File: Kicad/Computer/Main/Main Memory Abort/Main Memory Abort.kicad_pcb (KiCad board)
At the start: 2 copper layers, 18.8 x 43.3 mm, 14 parts, among them IC1 AP7365-33WG-7, IC2 74LVC32APW,118, IC4 74LVC74APW,118, IC5 SN74CBT3257CPWR, IC7 74LVC11PW,112, J2 Conn_02x16_Counter_Clockwise

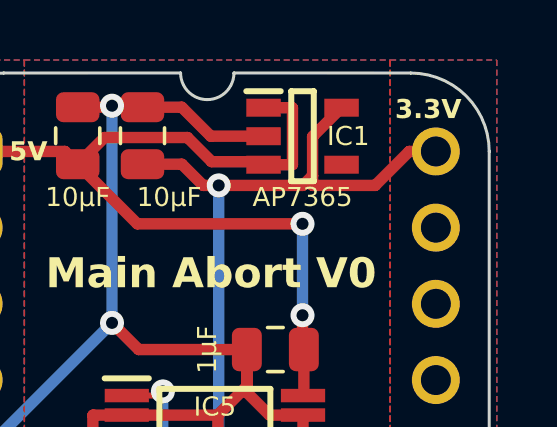
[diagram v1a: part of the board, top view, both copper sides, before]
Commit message: Added a (potentially) 50MHz board.
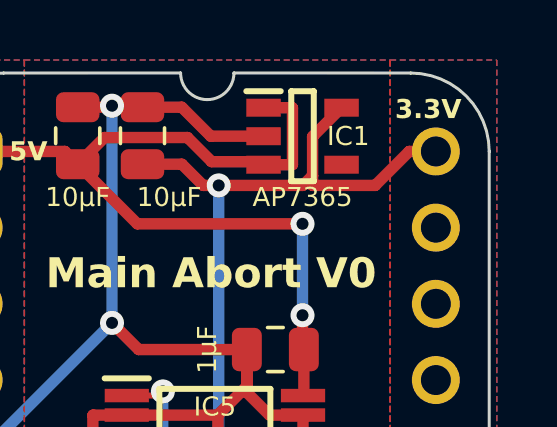
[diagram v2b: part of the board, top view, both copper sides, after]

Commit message: Started adding SD Card writing.
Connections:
- net ~{ABORT} renamed ~{Contention}
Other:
- board text added: "~{FAIL}"
- board text removed: "~{ABORT}"
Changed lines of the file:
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@@
 	(net 39 "~{Main}_{2}")
 	(net 40 "~{Reset}")
-	(net 41 "~{ABORT}")
+	(net 41 "~{Contention}")
 	(net 42 "~{Main}_{M}")
 	(footprint "SamacSys_Parts:C_0805"
@@
 		(fp_arc
 			(start 14.404267 -2.613733)
-			(mid 16.252453 -1.848189)
+			(mid 16.25245 -1.848186)
 			(end 17.017999 -0.000001)
 			(stroke
@@
 			(layers "*.Cu" "*.Mask")
 			(remove_unused_layers no)
-			(net 41 "~{ABORT}")
+			(net 41 "~{Contention}")
 			(pinfunction "Pin_19")
 			(pintype "passive")
@@
 			(size 0.45 1.475)
 			(layers "F.Cu" "F.Paste" "F.Mask")
-			(net 41 "~{ABORT}")
+			(net 41 "~{Contention}")
 			(pinfunction "~{1Q}")
 			(pintype "output")
@@
 		)
 	)
-	(gr_text "~{ABORT}"
+	(gr_text "~{FAIL}"
 		(at 103.124 91.44 0)
 		(layer "F.SilkS")

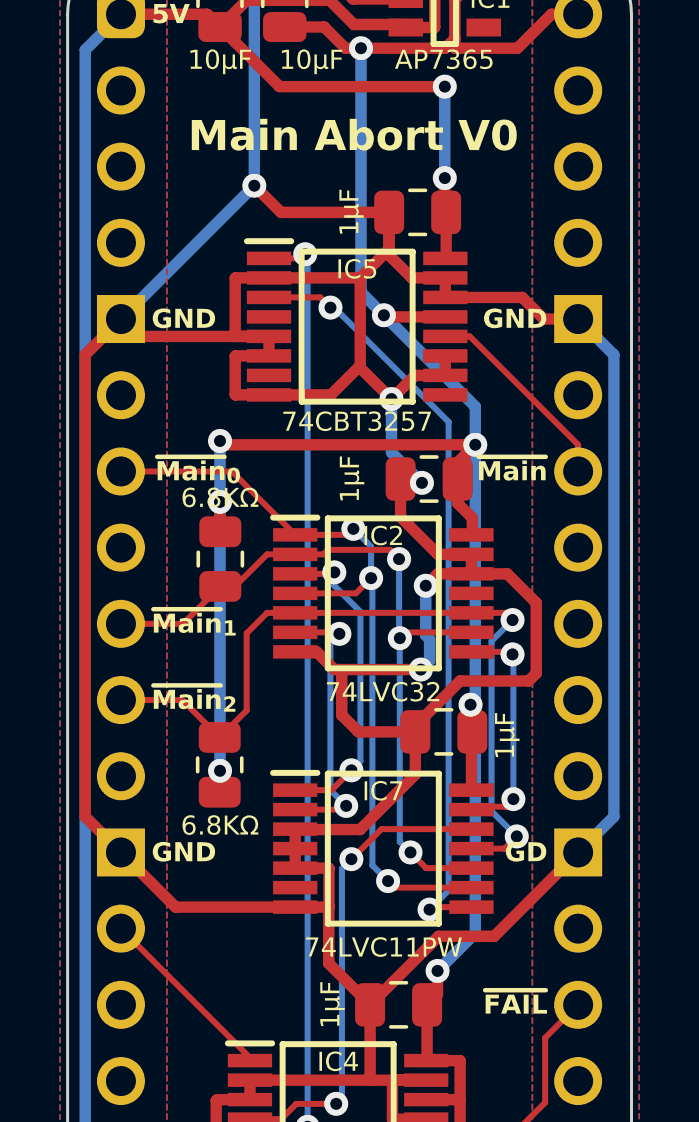
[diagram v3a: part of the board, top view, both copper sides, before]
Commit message: Added a TTL5V UART.
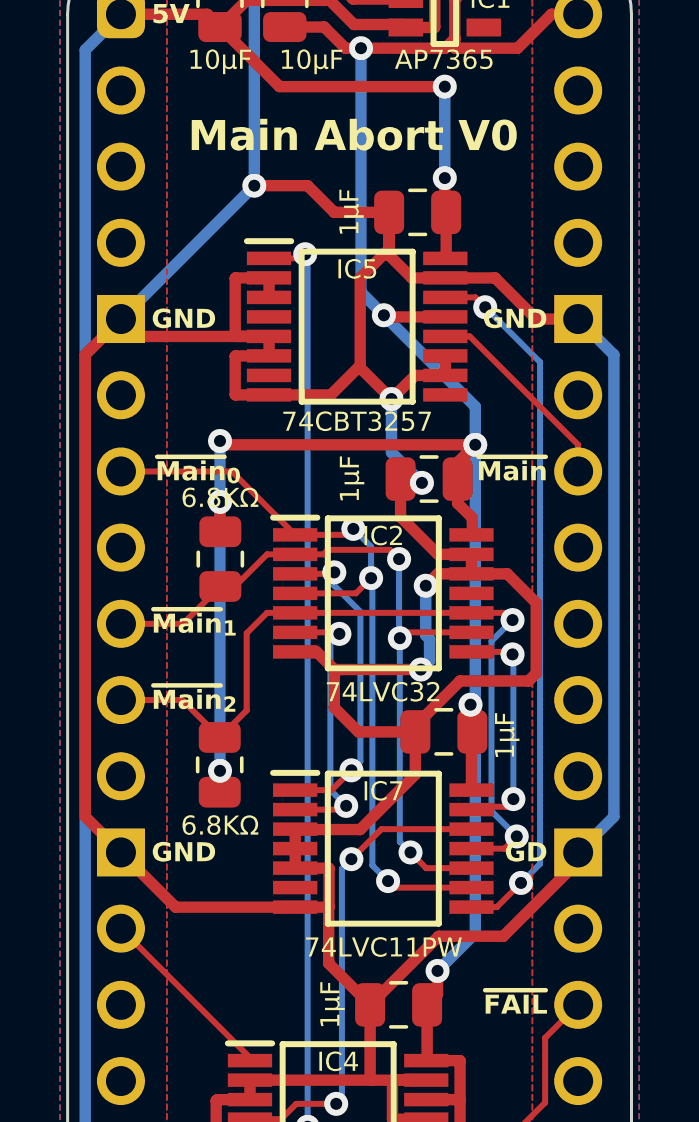
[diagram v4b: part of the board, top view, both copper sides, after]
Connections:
- net Net-(IC2-1Y) renamed /~{Main}+~{Main}_{1}
- net Net-(IC2-2Y) renamed /~{Main}+~{Main}_{2}
- net Net-(IC2-3Y) renamed /~{Main}_{1}+~{Main}_{2}
- IC5 pad 14: GND -> Net-(IC5-4B1)
- IC5 pad 3: Net-(IC5-1B2) -> GND
- IC7 pad 8: Net-(IC5-1B2) -> Net-(IC5-4B1)
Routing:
- net Net-(IC5-1B2): track 25.7 -> 0.00 mm, vias 2 -> 0
- net Net-(IC5-4B1): track 0.00 -> 23.7 mm, vias 0 -> 2
- net GND: track 180.7 -> 177.7 mm
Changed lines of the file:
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@@
 	(net 0 "")
 	(net 1 "unconnected-(IC1-ADJ-Pad4)")
-	(net 2 "Net-(IC2-1Y)")
-	(net 3 "Net-(IC2-2Y)")
-	(net 4 "Net-(IC2-3Y)")
+	(net 2 "/~{Main}+~{Main}_{1}")
+	(net 3 "/~{Main}+~{Main}_{2}")
+	(net 4 "/~{Main}_{1}+~{Main}_{2}")
 	(net 5 "unconnected-(IC2-4Y-Pad11)")
 	(net 6 "Net-(IC4-1Q)")
@@
 	(net 9 "unconnected-(IC5-2A-Pad7)")
 	(net 10 "unconnected-(IC5-3A-Pad9)")
-	(net 11 "Net-(IC5-1B2)")
+	(net 11 "Net-(IC5-4B1)")
 	(net 12 "unconnected-(IC5-1A-Pad4)")
 	(net 13 "Net-(IC4-~{1SD})")
@@
 			(size 0.45 1.475)
 			(layers "F.Cu" "F.Paste" "F.Mask")
-			(net 2 "Net-(IC2-1Y)")
+			(net 2 "/~{Main}+~{Main}_{1}")
 			(pinfunction "1Y")
 			(pintype "passive")
@@
 			(size 0.45 1.475)
 			(layers "F.Cu" "F.Paste" "F.Mask")
-			(net 3 "Net-(IC2-2Y)")
+			(net 3 "/~{Main}+~{Main}_{2}")
 			(pinfunction "2Y")
 			(pintype "passive")
@@
 			(size 0.45 1.475)
 			(layers "F.Cu" "F.Paste" "F.Mask")
-			(net 4 "Net-(IC2-3Y)")
+			(net 4 "/~{Main}_{1}+~{Main}_{2}")
 			(pinfunction "3Y")
 			(pintype "passive")
@@
 			(size 0.45 1.475)
 			(layers "F.Cu" "F.Paste" "F.Mask")
-			(net 2 "Net-(IC2-1Y)")
+			(net 2 "/~{Main}+~{Main}_{1}")
 			(pinfunction "1A")
 			(pintype "passive")
@@
 			(size 0.45 1.475)
 			(layers "F.Cu" "F.Paste" "F.Mask")
-			(net 3 "Net-(IC2-2Y)")
+			(net 3 "/~{Main}+~{Main}_{2}")
 			(pinfunction "1B")
 			(pintype "passive")
@@
 			(size 0.45 1.475)
 			(layers "F.Cu" "F.Paste" "F.Mask")
-			(net 11 "Net-(IC5-1B2)")
+			(net 11 "Net-(IC5-4B1)")
 			(pinfunction "3Y")
 			(pintype "passive")
@@
 			(size 0.45 1.475)
 			(layers "F.Cu" "F.Paste" "F.Mask")
-			(net 4 "Net-(IC2-3Y)")
+			(net 4 "/~{Main}_{1}+~{Main}_{2}")
 			(pinfunction "1C")
 			(pintype "passive")
@@
 		(fp_arc
 			(start 14.404267 -2.613733)
-			(mid 16.25245 -1.848186)
+			(mid 16.252451 -1.848184)
 			(end 17.017999 -0.000001)
 			(stroke
@@
 			(size 0.45 1.475)
 			(layers "F.Cu" "F.Paste" "F.Mask")
-			(net 11 "Net-(IC5-1B2)")
+			(net 35 "GND")
 			(pinfunction "1B2")
 			(pintype "tri_state")
@@
 			(size 0.45 1.475)
 			(layers "F.Cu" "F.Paste" "F.Mask")
-			(net 35 "GND")
+			(net 11 "Net-(IC5-4B1)")
 			(pinfunction "4B1")
 			(pintype "tri_state")
@@
 	)
 	(segment
-		(start 99.269 88.183)
-		(end 99.187 88.265)
+		(start 100.714123 67.859)
+		(end 99.712 67.859)
 		(width 0.2)
 		(layer "F.Cu")
@@
 	)
 	(segment
-		(start 100.584 88.183)
-		(end 99.269 88.183)
+		(start 101.041508 68.186385)
+		(end 100.714123 67.859)
 		(width 0.2)
 		(layer "F.Cu")
@@
 	)
 	(segment
-		(start 95.545 67.859)
-		(end 95.885 68.199)
+		(start 100.584 88.183)
+		(end 101.428 88.183)
 		(width 0.2)
 		(layer "F.Cu")
@@
 	)
 	(segment
-		(start 93.836 67.859)
-		(end 95.545 67.859)
+		(start 101.428 88.183)
+		(end 102.235 87.376)
 		(width 0.2)
 		(layer "F.Cu")
@@
 	)
 	(via
-		(at 95.885 68.199)
+		(at 102.235 87.376)
 		(size 0.8)
 		(drill 0.4)
@@
 	)
 	(via
-		(at 99.187 88.265)
+		(at 101.041508 68.186385)
 		(size 0.8)
 		(drill 0.4)
@@
 	)
 	(segment
-		(start 99.822 72.009)
-		(end 96.012 68.199)
-		(width 0.2)
-		(layer "B.Cu")
-		(net 11)
-	)
-	(segment
-		(start 99.187 88.265)
-		(end 99.822 87.63)
+		(start 102.235 87.376)
+		(end 102.87 86.741)
 		(width 0.2)
 		(layer "B.Cu")
@@
 	)
 	(segment
-		(start 96.012 68.199)
-		(end 95.885 68.199)
+		(start 102.87 70.014877)
+		(end 101.041508 68.186385)
 		(width 0.2)
 		(layer "B.Cu")
@@
 	)
 	(segment
-		(start 99.822 87.63)
-		(end 99.822 72.009)
+		(start 102.87 86.741)
+		(end 102.87 70.014877)
 		(width 0.2)
 		(layer "B.Cu")
@@
 	)
 	(segment
+		(start 96.819 82.341)
+		(end 98.712 82.341)
+		(width 0.38)
+		(layer "F.Cu")
+		(net 35)
+	)
+	(segment
 		(start 94.708 88.183)
 		(end 90.723 88.183)
@@
 	)
 	(segment
-		(start 100.203 80.645)
-		(end 98.712 82.136)
+		(start 95.123 64.135)
+		(end 93.345 64.135)
 		(width 0.38)
 		(layer "F.Cu")
@@
 	)
 	(segment
-		(start 97.84 66.4545)
-		(end 98.5945 67.209)
+		(start 100.203 80.645)
+		(end 98.712 82.136)
 		(width 0.38)
 		(layer "F.Cu")
@@
 	)
 	(segment
-		(start 99.712 67.209)
-		(end 99.712 67.859)
+		(start 97.84 66.4545)
+		(end 98.5945 67.209)
 		(width 0.38)
 		(layer "F.Cu")
@@
 	)
 	(segment
+		(start 99.712 67.209)
+		(end 101.372 67.209)
+		(width 0.38)
+		(layer "F.Cu")
+		(net 35)
+	)
+	(segment
 		(start 99.077 93.95)
 		(end 97.9595 93.95)
@@
 	)
 	(segment
-		(start 93.836 69.159)
-		(end 93.836 69.809)
+		(start 99.491 89.154)
+		(end 97.205 91.44)
 		(width 0.38)
 		(layer "F.Cu")
@@
 	)
 	(segment
-		(start 96.875 70.13)
-		(end 95.896 71.109)
+		(start 93.836 69.159)
+		(end 93.836 69.809)
 		(width 0.38)
 		(layer "F.Cu")
@@
 	)
 	(segment
-		(start 102.276 67.859)
-		(end 102.997 68.58)
+		(start 96.875 70.13)
+		(end 95.896 71.109)
 		(width 0.38)
 		(layer "F.Cu")
@@
 	)
 	(segment
-		(start 96.258869 80.264)
-		(end 96.258869 81.780869)
-		(width 0.38)
-		(layer "F.Cu")
-		(net 35)
-	)
-	(segment
-		(start 99.712 67.859)
-		(end 102.276 67.859)
-		(width 0.38)
-		(layer "F.Cu")
-		(net 35)
-	)
-	(segment
 		(start 87.71 69.77)
 		(end 87.71 85.17)
@@
 	)
 	(segment
-		(start 97.84 66.244)
-		(end 96.875 67.209)
+		(start 96.012 65.024)
+		(end 95.123 64.135)
 		(width 0.38)
 		(layer "F.Cu")
@@
 	)
 	(segment
-		(start 104.14 86.36)
-		(end 101.346 89.154)
+		(start 97.84 66.244)
+		(end 96.875 67.209)
 		(width 0.38)
 		(layer "F.Cu")
@@
 	)
 	(segment
-		(start 102.997 68.58)
-		(end 104.14 68.58)
-		(width 0.38)
-		(layer "F.Cu")
-		(net 35)
-	)
-	(segment
 		(start 98.712 83.761329)
 		(end 98.712 82.341)
@@
 	)
 	(segment
-		(start 93.836 69.159)
-		(end 89.479 69.159)
+		(start 93.836 67.209)
+		(end 93.836 67.859)
 		(width 0.38)
 		(layer "F.Cu")
@@
 	)
 	(segment
-		(start 94.723 85.598)
-		(end 96.875329 85.598)
+		(start 93.836 69.159)
+		(end 89.479 69.159)
 		(width 0.38)
 		(layer "F.Cu")
@@
 	)
 	(segment
-		(start 101.346 89.154)
-		(end 99.491 89.154)
+		(start 94.723 85.598)
+		(end 96.875329 85.598)
 		(width 0.38)
 		(layer "F.Cu")
@@
 	)
 	(segment
-		(start 96.875 67.209)
-		(end 93.836 67.209)
+		(start 95.8355 86.893)
+		(end 95.8355 88.173)
 		(width 0.38)
 		(layer "F.Cu")
@@
 	)
 	(segment
-		(start 95.8355 86.893)
-		(end 95.8355 88.173)
+		(start 100.584 77.074)
+		(end 101.776915 77.074)
 		(width 0.38)
 		(layer "F.Cu")
@@
 	)
 	(segment
-		(start 100.584 77.074)
-		(end 101.776915 77.074)
+		(start 104.14 86.65894)
+		(end 101.64494 89.154)
 		(width 0.38)
 		(layer "F.Cu")
@@
 	)
 	(segment
-		(start 97.84 65.024)
-		(end 94.234 65.024)
-		(width 0.38)
-		(layer "F.Cu")
-		(net 35)
-	)
-	(segment
 		(start 92.7185 69.159)
 		(end 92.7085 69.149)
@@
 	)
 	(segment
-		(start 94.708 85.583)
-		(end 94.708 86.233)
+		(start 96.012 81.534)
+		(end 96.819 82.341)
 		(width 0.38)
 		(layer "F.Cu")
@@
 	)
 	(segment
-		(start 96.875 70.13)
-		(end 96.875 70.205)
+		(start 94.708 85.583)
+		(end 94.708 86.233)
 		(width 0.38)
 		(layer "F.Cu")
@@
 	)
 	(segment
-		(start 96.819 82.341)
-		(end 98.712 82.341)
+		(start 96.875 70.13)
+		(end 96.875 70.205)
 		(width 0.38)
 		(layer "F.Cu")
@@
 	)
 	(segment
+		(start 101.372 67.209)
+		(end 102.743 68.58)
+		(width 0.38)
+		(layer "F.Cu")
+		(net 35)
+	)
+	(segment
 		(start 94.708 86.233)
 		(end 94.708 86.883)
@@
 	)
 	(segment
+		(start 101.64494 89.154)
+		(end 99.491 89.154)
+		(width 0.38)
+		(layer "F.Cu")
+		(net 35)
+	)
+	(segment
 		(start 90.723 88.183)
 		(end 88.9 86.36)
@@
 	)
 	(segment
-		(start 94.234 65.024)
-		(end 93.345 64.135)
-		(width 0.38)
-		(layer "F.Cu")
-		(net 35)
-	)
-	(segment
 		(start 97.84 65.024)
 		(end 97.84 66.4545)
@@
 	)
 	(segment
-		(start 99.491 89.154)
-		(end 97.205 91.44)
-		(width 0.38)
-		(layer "F.Cu")
-		(net 35)
-	)
-	(segment
 		(start 100.584 76.424)
 		(end 100.584 76.835)
@@
 	)
 	(segment
-		(start 98.712 82.136)
-		(end 98.712 82.341)
-		(width 0.38)
-		(layer "F.Cu")
-		(net 35)
-	)
-	(segment
 		(start 94.708 86.883)
 		(end 95.8255 86.883)
@@
 	)
 	(segment
-		(start 96.258869 81.780869)
-		(end 96.819 82.341)
+		(start 97.84 65.024)
+		(end 96.012 65.024)
+		(width 0.38)
+		(layer "F.Cu")
+		(net 35)
+	)
+	(segment
+		(start 102.743 68.58)
+		(end 104.14 68.58)
+		(width 0.38)
+		(layer "F.Cu")
+		(net 35)
+	)
+	(segment
+		(start 96.012 80.264)
+		(end 96.012 81.534)
 		(width 0.38)
 		(layer "F.Cu")

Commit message: Generated Gerbers for the Mainboard Small and Components.
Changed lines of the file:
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@@
 		(fp_arc
 			(start 14.404267 -2.613733)
-			(mid 16.252451 -1.848184)
+			(mid 16.252448 -1.848183)
 			(end 17.017999 -0.000001)
 			(stroke
